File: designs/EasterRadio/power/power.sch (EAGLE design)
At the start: 23 parts, among them IC1 MCP73832T-2ACI_OT, IC2 TPS62160DGKR, IC3 DMP1045U-7, J1 10118192-0001LF, J2 S2B-PH-SM4

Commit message: added esd for rs232 to can
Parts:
- renumbered LED1 to C, LED2 to F
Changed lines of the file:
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@@
 <part name="IC1" library="MouserUseful" deviceset="MCP73832T-2ACI_OT" device=""/>
 <part name="C2" library="CommonParts" deviceset="C-EU_1206" device="C1206" package3d_urn="urn:adsk.eagle:package:23618/2" value="4.7uF"/>
-<part name="LED1" library="CommonParts" deviceset="LED_1206" device="SMT1206" package3d_urn="urn:adsk.eagle:package:15796/2"/>
+<part name="C" library="CommonParts" deviceset="LED_1206" device="SMT1206" package3d_urn="urn:adsk.eagle:package:15796/2"/>
 <part name="C1" library="CommonParts" deviceset="C-EU_1206" device="C1206" package3d_urn="urn:adsk.eagle:package:23618/2" value="4.7uF"/>
 <part name="GND4" library="supply1" library_urn="urn:adsk.eagle:library:371" deviceset="GNDA" device=""/>
@@
 <part name="R3" library="CommonParts" deviceset="R-EU_805" device="R0805" package3d_urn="urn:adsk.eagle:package:23553/2" value="470ohm"/>
 <part name="R2" library="CommonParts" deviceset="R-EU_805" device="R0805" package3d_urn="urn:adsk.eagle:package:23553/2" value="470ohm"/>
-<part name="LED2" library="CommonParts" deviceset="LED_1206" device="SMT1206" package3d_urn="urn:adsk.eagle:package:15796/2"/>
+<part name="F" library="CommonParts" deviceset="LED_1206" device="SMT1206" package3d_urn="urn:adsk.eagle:package:15796/2"/>
 <part name="GND1" library="supply1" library_urn="urn:adsk.eagle:library:371" deviceset="GNDA" device=""/>
 <part name="R1" library="CommonParts" deviceset="R-EU_805" device="R0805" package3d_urn="urn:adsk.eagle:package:23553/2"/>
@@
 <attribute name="VALUE" x="77.216" y="107.569" size="1.778" layer="96" rot="R180"/>
 </instance>
-<instance part="LED1" gate="G$1" x="24.13" y="91.44" smashed="yes" rot="R90">
+<instance part="C" gate="G$1" x="24.13" y="91.44" smashed="yes" rot="R90">
 <attribute name="NAME" x="26.162" y="87.376" size="1.778" layer="95" rot="R180"/>
 <attribute name="VALUE" x="28.702" y="97.155" size="1.778" layer="96" rot="R180"/>
@@
 <attribute name="VALUE" x="31.75" y="95.758" size="1.778" layer="96"/>
 </instance>
-<instance part="LED2" gate="G$1" x="26.67" y="99.06" smashed="yes" rot="R270">
+<instance part="F" gate="G$1" x="26.67" y="99.06" smashed="yes" rot="R270">
 <attribute name="NAME" x="19.558" y="95.504" size="1.778" layer="95"/>
 <attribute name="VALUE" x="22.098" y="93.345" size="1.778" layer="96"/>
@@
 <segment>
 <pinref part="GND1" gate="1" pin="GNDA"/>
-<pinref part="LED2" gate="G$1" pin="C"/>
+<pinref part="F" gate="G$1" pin="C"/>
 <wire x1="19.05" y1="99.06" x2="21.59" y2="99.06" width="0.1524" layer="91"/>
 </segment>
@@
 <net name="N$10" class="0">
 <segment>
-<pinref part="LED1" gate="G$1" pin="C"/>
+<pinref part="C" gate="G$1" pin="C"/>
 <wire x1="30.48" y1="91.44" x2="29.21" y2="91.44" width="0.1524" layer="91"/>
 <pinref part="R3" gate="G$1" pin="1"/>
@@
 <wire x1="124.46" y1="113.03" x2="124.46" y2="129.54" width="0.1524" layer="91"/>
 <junction x="124.46" y="129.54"/>
-<pinref part="LED1" gate="G$1" pin="A"/>
+<pinref part="C" gate="G$1" pin="A"/>
 <wire x1="21.59" y1="91.44" x2="12.7" y2="91.44" width="0.1524" layer="91"/>
 <junction x="12.7" y="91.44"/>
@@
 <pinref part="R2" gate="G$1" pin="1"/>
 <wire x1="30.48" y1="99.06" x2="29.21" y2="99.06" width="0.1524" layer="91"/>
-<pinref part="LED2" gate="G$1" pin="A"/>
-</segment>
-</net>
+<pinref part="F" gate="G$1" pin="A"/>
+</segment>
+</net>

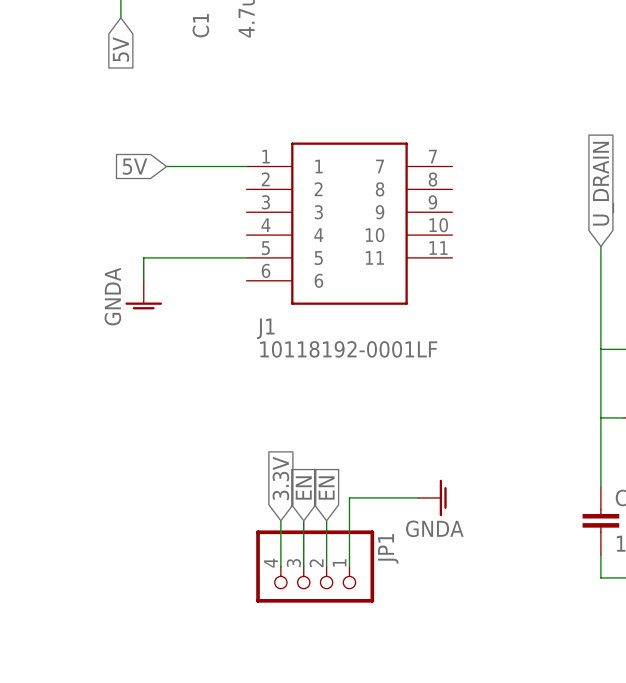
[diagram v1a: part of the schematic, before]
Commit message: added mainboard layout and new 3.5mm jack
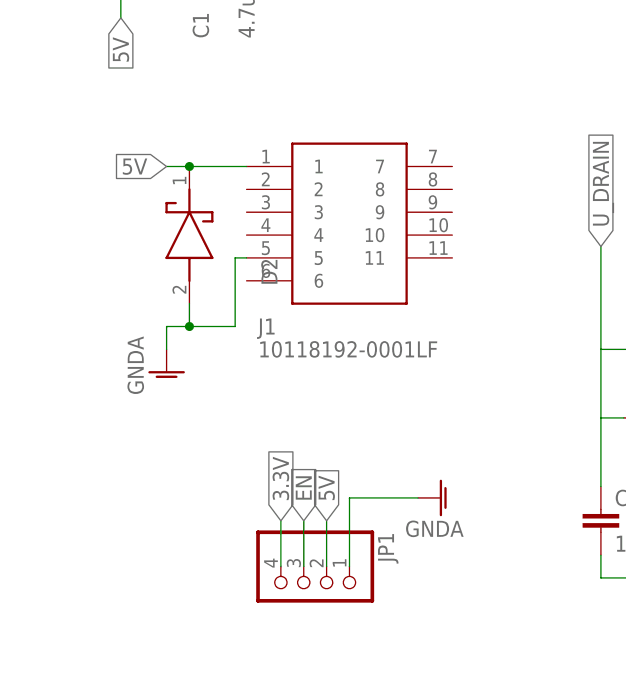
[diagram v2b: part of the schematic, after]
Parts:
- added D2: LSM115JE3_TR13, CommonParts:LSM115JE3_TR13
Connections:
- net 5V: now also D2.K, JP1.2
- net EN: no longer JP1.2
- net GNDA: now also D2.A
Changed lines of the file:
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@@
 <setting verticaltext="up"/>
 </settings>
-<grid distance="0.1" unitdist="inch" unit="inch" style="lines" multiple="1" display="no" altdistance="0.01" altunitdist="inch" altunit="inch"/>
+<grid distance="0.05" unitdist="inch" unit="inch" style="lines" multiple="1" display="no" altdistance="0.01" altunitdist="inch" altunit="inch"/>
 <layers>
 <layer number="1" name="Top" color="4" fill="1" visible="no" active="no"/>
@@
 <part name="JP1" library="pinhead" library_urn="urn:adsk.eagle:library:325" deviceset="PINHD-1X4" device="" package3d_urn="urn:adsk.eagle:package:22407/2"/>
 <part name="GND7" library="supply1" library_urn="urn:adsk.eagle:library:371" deviceset="GNDA" device=""/>
+<part name="D2" library="CommonParts" deviceset="LSM115JE3_TR13" device=""/>
 </parts>
 <sheets>
@@
 <attribute name="VALUE" x="27.94" y="39.37" size="1.778" layer="96" align="center-left"/>
 </instance>
-<instance part="GND2" gate="1" x="15.24" y="44.45" smashed="yes">
-<attribute name="VALUE" x="12.7" y="41.91" size="1.778" layer="96" rot="R90"/>
+<instance part="GND2" gate="1" x="17.78" y="36.83" smashed="yes">
+<attribute name="VALUE" x="15.24" y="34.29" size="1.778" layer="96" rot="R90"/>
 </instance>
 <instance part="IC2" gate="G$1" x="91.44" y="36.83" smashed="yes">
@@
 <instance part="GND7" gate="1" x="48.26" y="22.86" smashed="yes" rot="R90">
 <attribute name="VALUE" x="50.8" y="20.32" size="1.778" layer="96" rot="R180"/>
+</instance>
+<instance part="D2" gate="G$1" x="20.32" y="62.23" smashed="yes" rot="R270">
+<attribute name="NAME" x="29.21" y="49.53" size="1.778" layer="95" rot="R270" align="center-left"/>
 </instance>
 </instances>
@@
 </segment>
 <segment>
+<pinref part="GND2" gate="1" pin="GNDA"/>
+<wire x1="17.78" y1="39.37" x2="17.78" y2="41.91" width="0.1524" layer="91"/>
 <pinref part="J1" gate="G$1" pin="5"/>
-<wire x1="26.67" y1="49.53" x2="15.24" y2="49.53" width="0.1524" layer="91"/>
-<pinref part="GND2" gate="1" pin="GNDA"/>
-<wire x1="15.24" y1="46.99" x2="15.24" y2="49.53" width="0.1524" layer="91"/>
+<wire x1="26.67" y1="49.53" x2="25.4" y2="49.53" width="0.1524" layer="91"/>
+<wire x1="25.4" y1="49.53" x2="25.4" y2="41.91" width="0.1524" layer="91"/>
+<wire x1="25.4" y1="41.91" x2="20.32" y2="41.91" width="0.1524" layer="91"/>
+<wire x1="20.32" y1="41.91" x2="17.78" y2="41.91" width="0.1524" layer="91"/>
+<wire x1="20.32" y1="44.45" x2="20.32" y2="41.91" width="0.1524" layer="91"/>
+<junction x="20.32" y="41.91"/>
+<pinref part="D2" gate="G$1" pin="A"/>
 </segment>
 <segment>
@@
 <segment>
 <pinref part="J1" gate="G$1" pin="1"/>
-<wire x1="26.67" y1="59.69" x2="17.78" y2="59.69" width="0.1524" layer="91"/>
+<wire x1="26.67" y1="59.69" x2="20.32" y2="59.69" width="0.1524" layer="91"/>
 <label x="17.78" y="59.69" size="1.778" layer="95" rot="R180" xref="yes"/>
+<pinref part="D2" gate="G$1" pin="K"/>
+<wire x1="20.32" y1="59.69" x2="17.78" y2="59.69" width="0.1524" layer="91"/>
+<junction x="20.32" y="59.69"/>
+</segment>
+<segment>
+<pinref part="JP1" gate="A" pin="2"/>
+<wire x1="35.56" y1="15.24" x2="35.56" y2="20.32" width="0.1524" layer="91"/>
+<label x="35.56" y="20.32" size="1.778" layer="95" rot="R90" xref="yes"/>
 </segment>
 </net>
@@
 </segment>
 <segment>
-<pinref part="JP1" gate="A" pin="2"/>
-<wire x1="35.56" y1="15.24" x2="35.56" y2="20.32" width="0.1524" layer="91"/>
-<label x="35.56" y="20.32" size="1.778" layer="95" rot="R90" xref="yes"/>
-</segment>
-<segment>

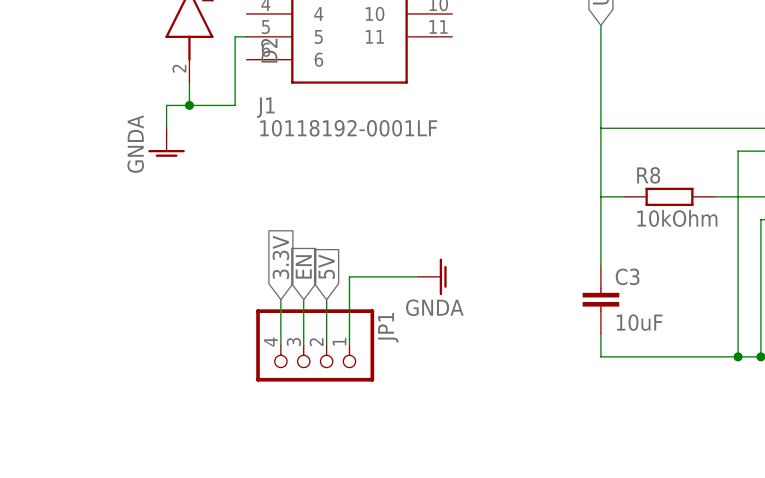
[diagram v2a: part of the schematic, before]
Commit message: added more stuff to pcb main for radio
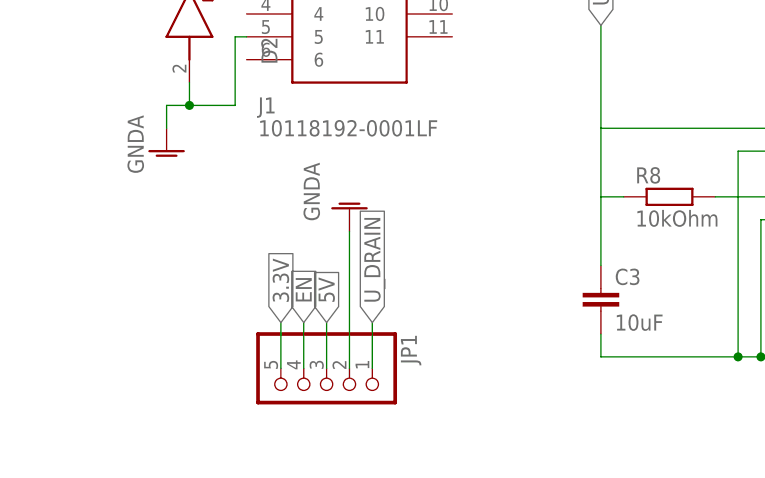
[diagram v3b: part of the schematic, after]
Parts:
- JP1: device pinhead:PINHD-1X4 -> pinhead:PINHD-1X5
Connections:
- net 3.3V: now also JP1.5; no longer JP1.4
- net 5V: now also JP1.3; no longer JP1.2
- net EN: now also JP1.4; no longer JP1.3
- net GNDA: now also JP1.2; no longer JP1.1
- net U_DRAIN: now also JP1.1
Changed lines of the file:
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@@
 <setting verticaltext="up"/>
 </settings>
-<grid distance="0.05" unitdist="inch" unit="inch" style="lines" multiple="1" display="no" altdistance="0.01" altunitdist="inch" altunit="inch"/>
+<grid distance="0.1" unitdist="inch" unit="inch" style="lines" multiple="1" display="no" altdistance="0.01" altunitdist="inch" altunit="inch"/>
 <layers>
 <layer number="1" name="Top" color="4" fill="1" visible="no" active="no"/>
@@
 <part name="GND6" library="supply1" library_urn="urn:adsk.eagle:library:371" deviceset="GNDA" device=""/>
 <part name="R8" library="CommonParts" deviceset="R-EU_805" device="R0805" package3d_urn="urn:adsk.eagle:package:23553/2" value="10kOhm"/>
-<part name="JP1" library="pinhead" library_urn="urn:adsk.eagle:library:325" deviceset="PINHD-1X4" device="" package3d_urn="urn:adsk.eagle:package:22407/2"/>
+<part name="D2" library="CommonParts" deviceset="LSM115JE3_TR13" device=""/>
+<part name="JP1" library="pinhead" library_urn="urn:adsk.eagle:library:325" deviceset="PINHD-1X5" device="" package3d_urn="urn:adsk.eagle:package:22469/2"/>
 <part name="GND7" library="supply1" library_urn="urn:adsk.eagle:library:371" deviceset="GNDA" device=""/>
-<part name="D2" library="CommonParts" deviceset="LSM115JE3_TR13" device=""/>
 </parts>
 <sheets>
@@
 <attribute name="VALUE" x="69.85" y="28.448" size="1.778" layer="96"/>
 </instance>
-<instance part="JP1" gate="A" x="33.02" y="12.7" smashed="yes" rot="R270">
-<attribute name="NAME" x="41.275" y="19.05" size="1.778" layer="95" rot="R270"/>
-<attribute name="VALUE" x="25.4" y="19.05" size="1.778" layer="96" rot="R270"/>
-</instance>
-<instance part="GND7" gate="1" x="48.26" y="22.86" smashed="yes" rot="R90">
-<attribute name="VALUE" x="50.8" y="20.32" size="1.778" layer="96" rot="R180"/>
-</instance>
 <instance part="D2" gate="G$1" x="20.32" y="62.23" smashed="yes" rot="R270">
 <attribute name="NAME" x="29.21" y="49.53" size="1.778" layer="95" rot="R270" align="center-left"/>
+</instance>
+<instance part="JP1" gate="A" x="35.56" y="10.16" smashed="yes" rot="R270">
+<attribute name="NAME" x="43.815" y="16.51" size="1.778" layer="95" rot="R270"/>
+<attribute name="VALUE" x="25.4" y="16.51" size="1.778" layer="96" rot="R270"/>
+</instance>
+<instance part="GND7" gate="1" x="38.1" y="30.48" smashed="yes" rot="R180">
+<attribute name="VALUE" x="33.02" y="35.56" size="1.778" layer="96" rot="R270"/>
 </instance>
 </instances>
@@
 </segment>
 <segment>
-<pinref part="JP1" gate="A" pin="1"/>
-<wire x1="38.1" y1="15.24" x2="38.1" y2="22.86" width="0.1524" layer="91"/>
-<wire x1="38.1" y1="22.86" x2="45.72" y2="22.86" width="0.1524" layer="91"/>
+<pinref part="JP1" gate="A" pin="2"/>
 <pinref part="GND7" gate="1" pin="GNDA"/>
+<wire x1="38.1" y1="12.7" x2="38.1" y2="27.94" width="0.1524" layer="91"/>
 </segment>
 </net>
@@
 </segment>
 <segment>
-<pinref part="JP1" gate="A" pin="2"/>
-<wire x1="35.56" y1="15.24" x2="35.56" y2="20.32" width="0.1524" layer="91"/>
-<label x="35.56" y="20.32" size="1.778" layer="95" rot="R90" xref="yes"/>
+<wire x1="35.56" y1="12.7" x2="35.56" y2="17.78" width="0.1524" layer="91"/>
+<label x="35.56" y="17.78" size="1.778" layer="95" rot="R90" xref="yes"/>
+<pinref part="JP1" gate="A" pin="3"/>
 </segment>
 </net>
@@
 <pinref part="R8" gate="G$1" pin="1"/>
 <wire x1="68.58" y1="31.75" x2="66.04" y2="31.75" width="0.1524" layer="91"/>
+</segment>
+<segment>
+<pinref part="JP1" gate="A" pin="1"/>
+<wire x1="40.64" y1="12.7" x2="40.64" y2="17.78" width="0.1524" layer="91"/>
+<label x="40.64" y="17.78" size="1.778" layer="95" rot="R90" xref="yes"/>
 </segment>
 </net>
@@
 </segment>
 <segment>
-<pinref part="JP1" gate="A" pin="4"/>
-<wire x1="30.48" y1="15.24" x2="30.48" y2="20.32" width="0.1524" layer="91"/>
-<label x="30.48" y="20.32" size="1.778" layer="95" rot="R90" xref="yes"/>
+<wire x1="30.48" y1="12.7" x2="30.48" y2="17.78" width="0.1524" layer="91"/>
+<label x="30.48" y="17.78" size="1.778" layer="95" rot="R90" xref="yes"/>
+<pinref part="JP1" gate="A" pin="5"/>
 </segment>
 </net>
@@
 </segment>
 <segment>
-<pinref part="JP1" gate="A" pin="3"/>
-<wire x1="33.02" y1="15.24" x2="33.02" y2="20.32" width="0.1524" layer="91"/>
-<label x="33.02" y="20.32" size="1.778" layer="95" rot="R90" xref="yes"/>
-</segment>
-</net>
+<wire x1="33.02" y1="12.7" x2="33.02" y2="17.78" width="0.1524" layer="91"/>
+<label x="33.02" y="17.78" size="1.778" layer="95" rot="R90" xref="yes"/>
+<pinref part="JP1" gate="A" pin="4"/>
+</segment>
+</net>

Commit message: changed poti and encoder pcb to correct schematic and brd + mainboard change for push btn on rotary encoder
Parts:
- R5: value 68kOhm -> 562kOhm
- R6: value 22kOhm -> 180kOhm
- R8: value 10kOhm -> 200kOhm
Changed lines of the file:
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@@
 <part name="C5" library="MouserUseful" deviceset="GRM219R61C226ME15K" device="C0805K" package3d_urn="urn:adsk.eagle:package:23681/2" value="22uF"/>
 <part name="L1" library="MouserUseful" deviceset="VLS6045EX-221M" device=""/>
-<part name="R5" library="CommonParts" deviceset="R-EU_805" device="R0805" package3d_urn="urn:adsk.eagle:package:23553/2" value="68kOhm"/>
-<part name="R6" library="CommonParts" deviceset="R-EU_805" device="R0805" package3d_urn="urn:adsk.eagle:package:23553/2" value="22kOhm"/>
+<part name="R5" library="CommonParts" deviceset="R-EU_805" device="R0805" package3d_urn="urn:adsk.eagle:package:23553/2" value="562kOhm"/>
+<part name="R6" library="CommonParts" deviceset="R-EU_805" device="R0805" package3d_urn="urn:adsk.eagle:package:23553/2" value="180kOhm"/>
 <part name="R4" library="CommonParts" deviceset="R-EU_805" device="R0805" package3d_urn="urn:adsk.eagle:package:23553/2" value="100kOhm"/>
 <part name="GND5" library="supply1" library_urn="urn:adsk.eagle:library:371" deviceset="GNDA" device=""/>
@@
 <part name="R7" library="CommonParts" deviceset="R-EU_805" device="R0805" package3d_urn="urn:adsk.eagle:package:23553/2" value="100Kohm"/>
 <part name="GND6" library="supply1" library_urn="urn:adsk.eagle:library:371" deviceset="GNDA" device=""/>
-<part name="R8" library="CommonParts" deviceset="R-EU_805" device="R0805" package3d_urn="urn:adsk.eagle:package:23553/2" value="10kOhm"/>
+<part name="R8" library="CommonParts" deviceset="R-EU_805" device="R0805" package3d_urn="urn:adsk.eagle:package:23553/2" value="200kOhm"/>
 <part name="D2" library="CommonParts" deviceset="LSM115JE3_TR13" device=""/>
 <part name="JP1" library="pinhead" library_urn="urn:adsk.eagle:library:325" deviceset="PINHD-1X5" device="" package3d_urn="urn:adsk.eagle:package:22469/2"/>
